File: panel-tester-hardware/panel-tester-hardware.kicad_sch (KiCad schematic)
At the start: 25 parts, among them J1 Screw_Terminal_01x02, J2 Conn_01x02, J3 Conn_01x07, Q2 BS170, U1 MCP4921, U3 LM358, U4 INA219AxD

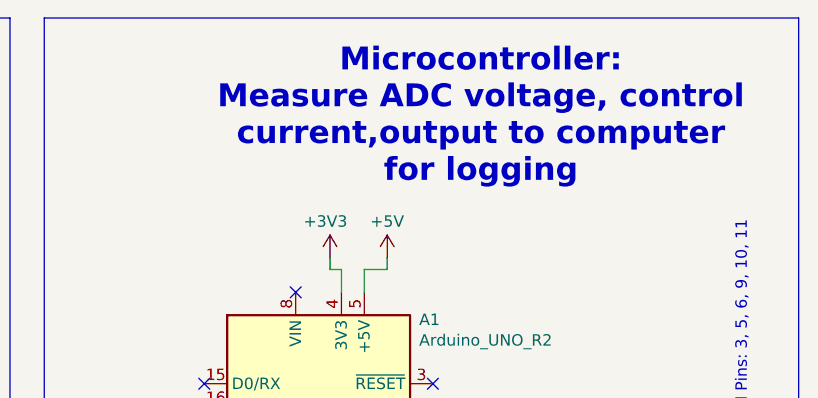
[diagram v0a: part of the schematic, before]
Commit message: Fix typos on schematic
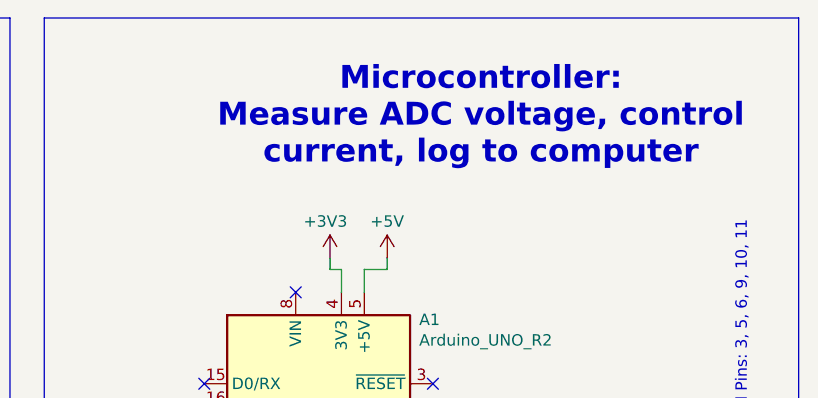
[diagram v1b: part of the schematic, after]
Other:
- note added: "Microcontroller: Measure ADC voltage, control current, log to computer"
- note removed: "Microcontroller: Measure ADC voltage, control current,output to computer for logging"
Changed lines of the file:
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@@
 		)
 	)
-	(text "Microcontroller:\nMeasure ADC voltage, control \ncurrent,output to computer \nfor logging"
+	(text "Microcontroller:\nMeasure ADC voltage, control \ncurrent, log to computer "
 		(exclude_from_sim no)
 		(at 230.124 26.162 0)

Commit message: Random changes to rev 2, before big changes
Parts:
- R11, R12, R5: now not fitted
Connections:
- net DAC_OUTPUT: now also C5.2, Q2.2 (G), R11.2
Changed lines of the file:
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@@
 	)
 	(junction
+		(at 114.3 59.69)
+		(diameter 0)
+		(color 0 0 0 0)
+	)
+	(junction
 		(at 163.83 82.55)
 		(diameter 0)
@@
 	)
 	(junction
+		(at 59.69 57.15)
+		(diameter 0)
+		(color 0 0 0 0)
+	)
+	(junction
 		(at 82.55 69.85)
 		(diameter 0)
@@
 	(wire
 		(pts
+			(xy 59.69 74.93) (xy 81.28 74.93)
+		)
+		(stroke
+			(width 0)
+			(type default)
+		)
+	)
+	(wire
+		(pts
 			(xy 40.64 41.91) (xy 40.64 44.45)
 		)
@@
 	(wire
 		(pts
+			(xy 81.28 66.04) (xy 114.3 66.04)
+		)
+		(stroke
+			(width 0)
+			(type default)
+		)
+	)
+	(wire
+		(pts
 			(xy 213.36 43.18) (xy 214.63 43.18)
 		)
@@
 	(wire
 		(pts
-			(xy 111.76 59.69) (xy 115.57 59.69)
+			(xy 111.76 59.69) (xy 114.3 59.69)
 		)
 		(stroke
@@
 	(wire
 		(pts
+			(xy 114.3 59.69) (xy 114.3 66.04)
+		)
+		(stroke
+			(width 0)
+			(type default)
+		)
+	)
+	(wire
+		(pts
 			(xy 151.13 46.99) (xy 154.94 46.99)
 		)
@@
 	(wire
 		(pts
+			(xy 114.3 59.69) (xy 115.57 59.69)
+		)
+		(stroke
+			(width 0)
+			(type default)
+		)
+	)
+	(wire
+		(pts
 			(xy 241.3 96.52) (xy 241.3 100.33)
 		)
@@
 	(wire
 		(pts
+			(xy 59.69 57.15) (xy 59.69 74.93)
+		)
+		(stroke
+			(width 0)
+			(type default)
+		)
+	)
+	(wire
+		(pts
 			(xy 109.22 69.85) (xy 116.84 69.85)
 		)
@@
 	(wire
 		(pts
+			(xy 81.28 74.93) (xy 81.28 66.04)
+		)
+		(stroke
+			(width 0)
+			(type default)
+		)
+	)
+	(wire
+		(pts
 			(xy 219.71 43.18) (xy 219.71 41.91)
 		)
@@
 	(wire
 		(pts
+			(xy 59.69 57.15) (xy 60.96 57.15)
+		)
+		(stroke
+			(width 0)
+			(type default)
+		)
+	)
+	(wire
+		(pts
 			(xy 212.09 102.87) (xy 212.09 101.6)
 		)
@@
 	(wire
 		(pts
-			(xy 58.42 57.15) (xy 60.96 57.15)
+			(xy 58.42 57.15) (xy 59.69 57.15)
 		)
 		(stroke
@@
 		(in_bom yes)
 		(on_board yes)
-		(dnp no)
+		(dnp yes)
 		(property "Reference" "R11"
 			(at 105.41 61.976 90)
@@
 		(in_bom yes)
 		(on_board yes)
-		(dnp no)
+		(dnp yes)
 		(fields_autoplaced yes)
 		(property "Reference" "R5"
@@
 		(in_bom yes)
 		(on_board yes)
-		(dnp no)
+		(dnp yes)
 		(property "Reference" "R12"
 			(at 105.41 72.136 90)
